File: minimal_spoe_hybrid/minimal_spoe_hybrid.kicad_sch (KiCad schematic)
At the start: 4 parts, among them J1 TBP02R2-381-03BE

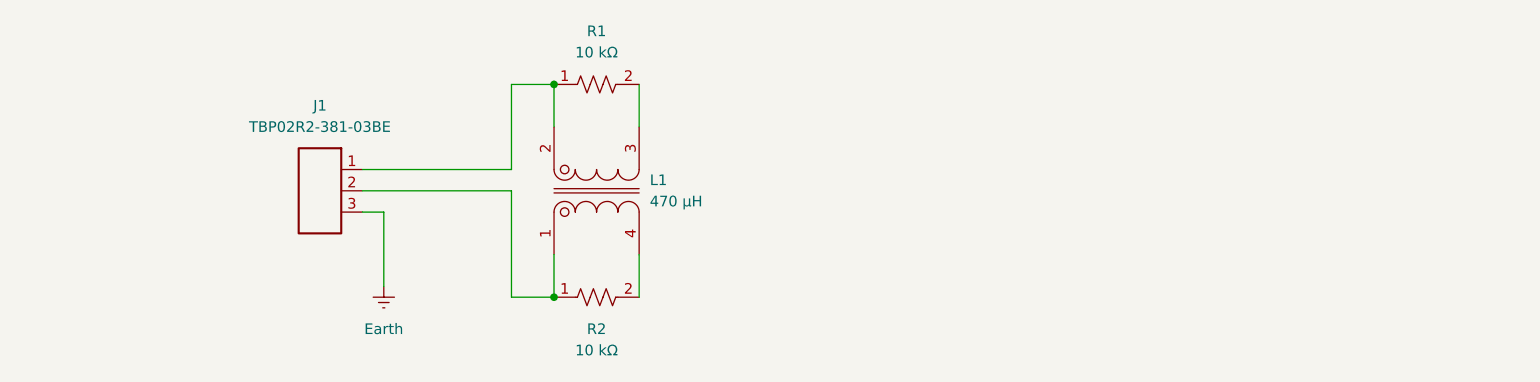
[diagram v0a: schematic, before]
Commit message: Update KiCAD Symbol Generator submodule and modify project settings
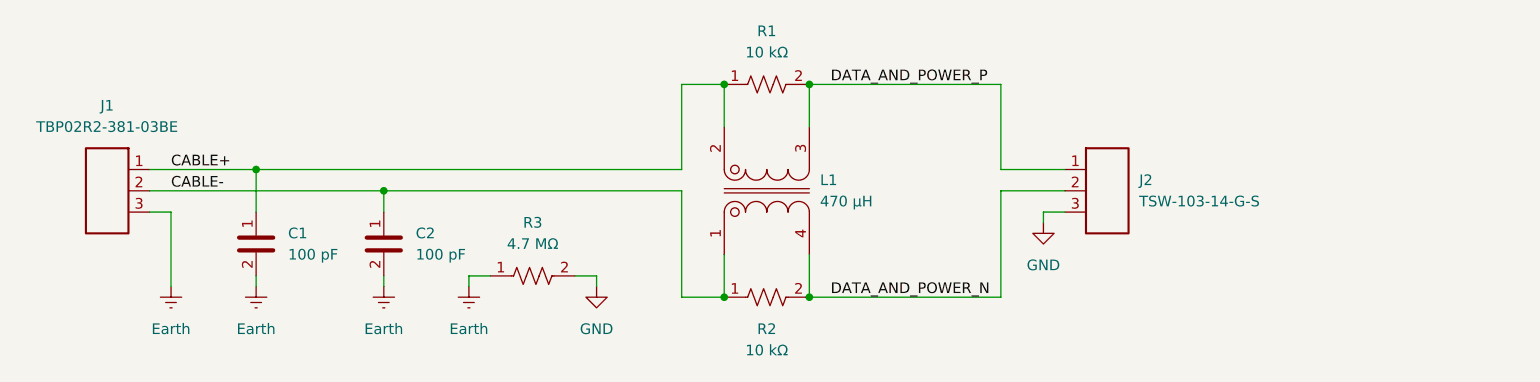
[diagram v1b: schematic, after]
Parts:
- added C1, C2: 100 pF, capacitor_footprints:C_1812_4532Metric, symbol UNITED_CAPACITORS_DATA_BASE:C_C1812C101JHGACTU
- added J2: TSW-103-14-G-S, connector_footprints:TSW-103-14-G-S, symbol UNITED_CONNECTORS_DATA_BASE:J_TSW-103-14-G-S
- added R3: 4.7 MΩ, resistor_footprints:R_2010_5025Metric, symbol UNITED_RESISTORS_DATA_BASE:R_CHV2010-JW-475ELF
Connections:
- net Earth: now also C1.2, C2.2, R3.1
- net CABLE-: now reaches J1.2, L1.1, R2.1
- net CABLE-: now also C2.1
- net DATA_AND_POWER_P: now reaches L1.2, R1.2
- net DATA_AND_POWER_P: now also J2.1
- net CABLE+: now reaches J1.1, L1.3, R1.1
- net CABLE+: now also C1.1
- net DATA_AND_POWER_N: now reaches L1.4, R2.2
- net DATA_AND_POWER_N: now also J2.2
- new net GND: J2.3, R3.2
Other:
- moved on the sheet: J1, L1, R1, R2

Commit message: Update KiCAD Symbol Generator submodule and modify project configuration
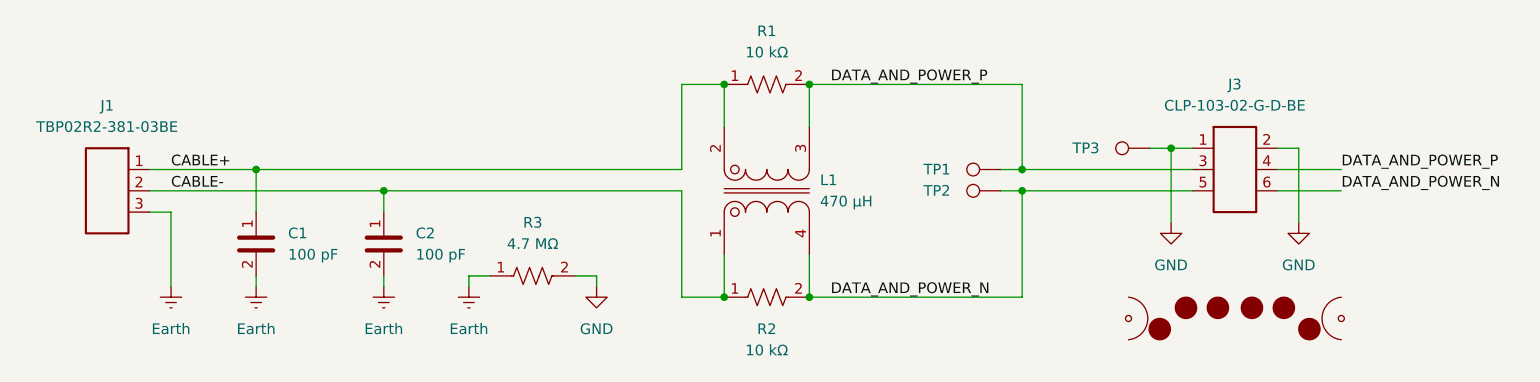
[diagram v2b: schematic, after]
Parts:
- removed J2: TSW-103-14-G-S, connector_footprints:TSW-103-14-G-S, symbol UNITED_CONNECTORS_DATA_BASE:J_TSW-103-14-G-S
- added J3: CLP-103-02-G-D-BE, connector_footprints:CLP-103-02-G-D-BE, symbol UNITED_CONNECTORS_DATA_BASE:J_CLP-103-02-G-D-BE
- added MB1: mouse-bite-midle-50mil-200mil, mouse_bite_footprints:mouse-bite-midle-50mil-250mil, symbol UNITED_MOUSE_BITES_DATA_BASE:mouse-bite-midle-50mil-250mil
- added TP1, TP2, TP3: TestPoint, test_point_footprints:TestPoint_THTPad_Castelated, symbol UNITED_TEST_POINTS:TestPoint_Castelated
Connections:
- net DATA_AND_POWER_N: now also J3.5, J3.6, TP2.1
- net DATA_AND_POWER_P: now also J3.3, J3.4, TP1.1
- net GND: now also J3.1, J3.2, TP3.1

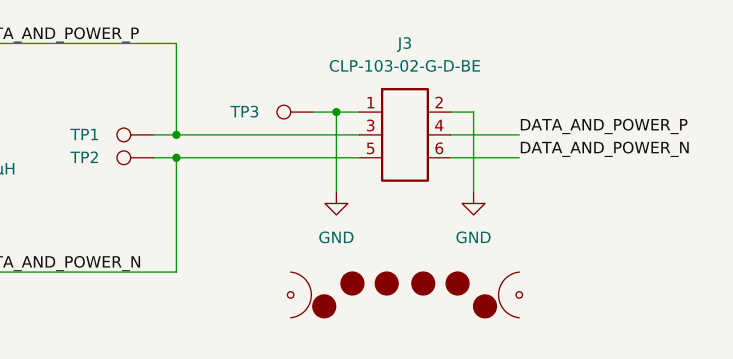
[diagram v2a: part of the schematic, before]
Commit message: Update KiCAD Symbol Generator submodule and remove unused circle elements from schematic
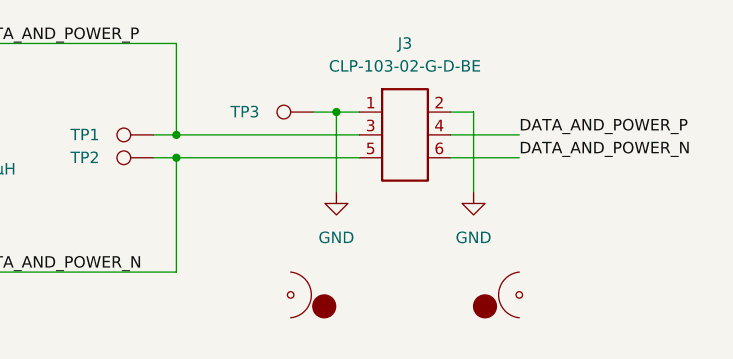
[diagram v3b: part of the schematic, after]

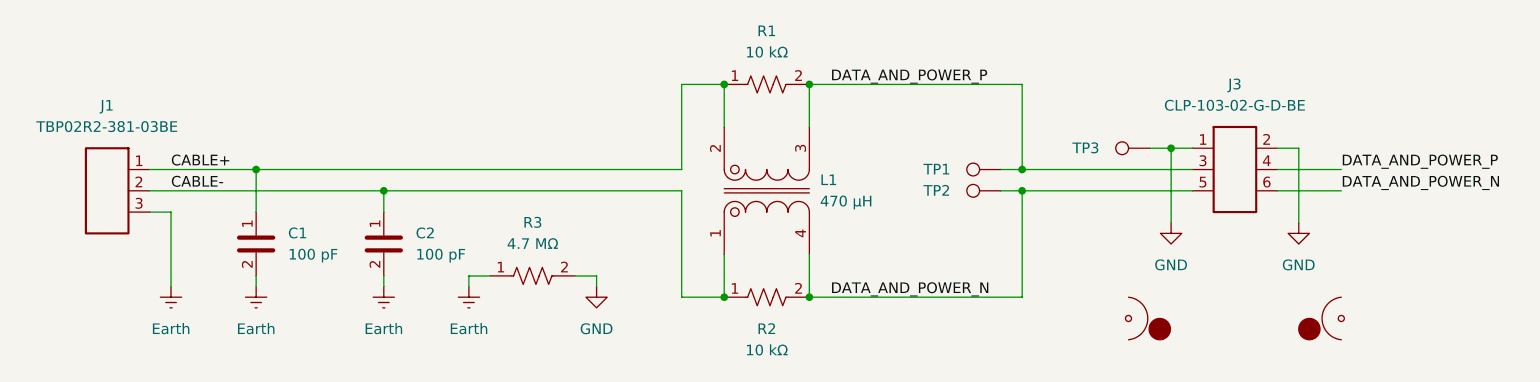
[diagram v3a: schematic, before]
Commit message: Update KiCAD Symbol Generator submodule and regenerate PDF schematic
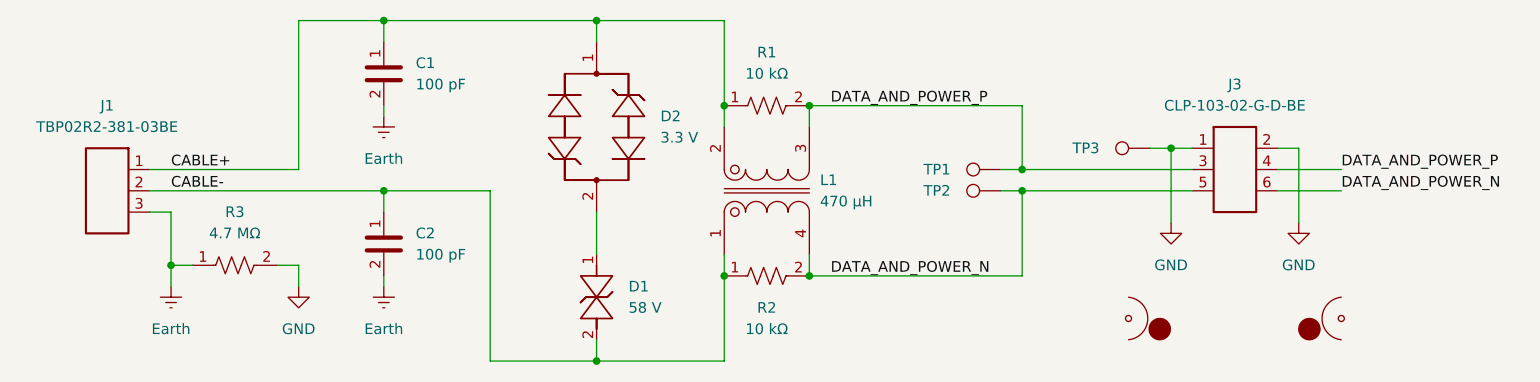
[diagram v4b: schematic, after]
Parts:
- added D1: 58 V, diode_footprints:DO-214AA, symbol UNITED_DIODES_DATA_BASE:D_SMBJ58CA
- added D2: 3.3 V, diode_footprints:SOD323, symbol UNITED_DIODES_DATA_BASE:D_SP4020-01FTG-C
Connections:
- net CABLE+: now also D2.1
- net CABLE-: now also D1.2
- new net: D1.1, D2.2
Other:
- moved on the sheet: C1, R1, R2, R3

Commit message: Add minimal_spoe_hybrid.glb and update KiCAD Symbol Generator submodule
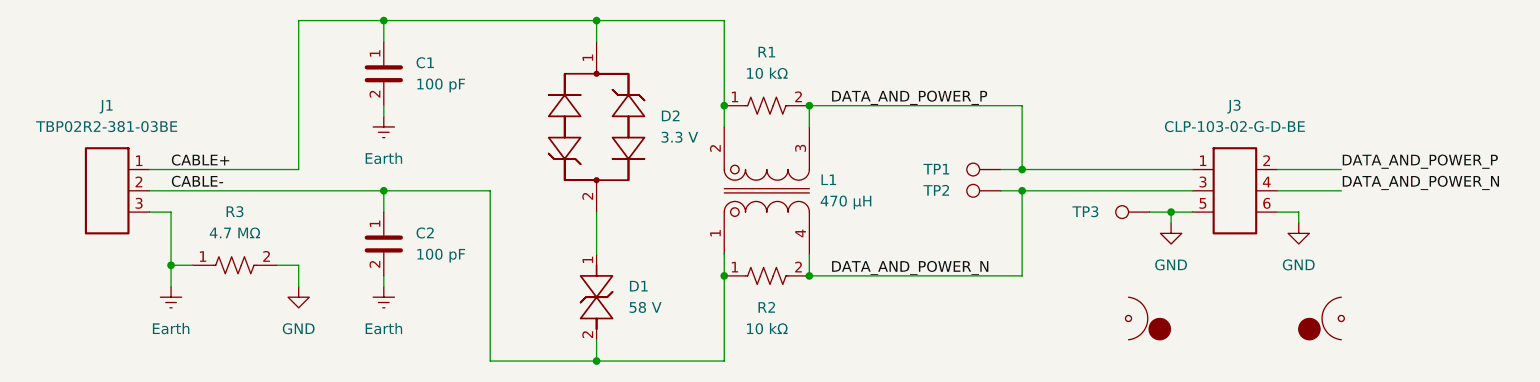
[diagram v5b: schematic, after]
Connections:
- net DATA_AND_POWER_N: now also J3.3, J3.4; no longer J3.5, J3.6
- net DATA_AND_POWER_P: now also J3.1, J3.2; no longer J3.3, J3.4
- net GND: now also J3.5, J3.6; no longer J3.1, J3.2
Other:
- moved on the sheet: J3, TP3
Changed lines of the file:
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@@
-	)
-	(junction
-		(at 195.58 96.52)
-		(diameter 0)
-		(color 0 0 0 0)
 	)
 	(junction
@@
 	)
 	(junction
+		(at 195.58 104.14)
+		(diameter 0)
+		(color 0 0 0 0)
+	)
+	(junction
 		(at 142.24 91.44)
 		(diameter 0)
@@
 	(wire
 		(pts
+			(xy 195.58 104.14) (xy 195.58 105.41)
+		)
+		(stroke
+			(width 0)
+			(type default)
+		)
+	)
+	(wire
+		(pts
 			(xy 101.6 91.44) (xy 101.6 92.71)
 		)
@@
 	(wire
 		(pts
+			(xy 208.28 104.14) (xy 210.82 104.14)
+		)
+		(stroke
+			(width 0)
+			(type default)
+		)
+	)
+	(wire
+		(pts
 			(xy 101.6 104.14) (xy 101.6 101.6)
 		)
@@
 	(wire
 		(pts
-			(xy 193.04 96.52) (xy 195.58 96.52)
-		)
-		(stroke
-			(width 0)
-			(type default)
-		)
-	)
-	(wire
-		(pts
 			(xy 127 121.92) (xy 142.24 121.92)
 		)
@@
 	(wire
 		(pts
+			(xy 195.58 104.14) (xy 198.12 104.14)
+		)
+		(stroke
+			(width 0)
+			(type default)
+		)
+	)
+	(wire
+		(pts
 			(xy 177.8 99.06) (xy 198.12 99.06)
 		)
@@
 	(wire
 		(pts
-			(xy 210.82 96.52) (xy 208.28 96.52)
-		)
-		(stroke
-			(width 0)
-			(type default)
-		)
-	)
-	(wire
-		(pts
-			(xy 195.58 96.52) (xy 195.58 105.41)
-		)
-		(stroke
-			(width 0)
-			(type default)
-		)
-	)
-	(wire
-		(pts
-			(xy 198.12 96.52) (xy 195.58 96.52)
+			(xy 193.04 104.14) (xy 195.58 104.14)
 		)
 		(stroke
@@
 	(wire
 		(pts
-			(xy 210.82 105.41) (xy 210.82 96.52)
+			(xy 210.82 105.41) (xy 210.82 104.14)
 		)
 		(stroke
@@
 	(symbol
 		(lib_id "UNITED_CONNECTORS_DATA_BASE:J_CLP-103-02-G-D-BE")
-		(at 203.2 99.06 0)
+		(at 203.2 101.6 0)
 		(unit 1)
 		(exclude_from_sim no)
@@
 		(fields_autoplaced yes)
 		(property "Reference" "J3"
-			(at 203.2 88.9 0)
+			(at 203.2 91.44 0)
 			(effects
 				(font
@@
 		)
 		(property "Value" "CLP-103-02-G-D-BE"
-			(at 203.2 91.44 0)
+			(at 203.2 93.98 0)
 			(effects
 				(font
@@
 		)
 		(property "Footprint" "connector_footprints:CLP-103-02-G-D-BE"
-			(at 208.28 107.95 0)
+			(at 208.28 110.49 0)
 			(show_name yes)
 			(effects
@@
 		)
 		(property "Datasheet" "https://suddendocs.samtec.com/catalog_english/clp_sm.pdf?_gl=1*1y4jlr9*_gcl_au*MTM0MTYyNTQ5MS4xNzM2MDk5MTUz*_ga*MTYxNDYyMTQ0Mi4xNzM2MDk5MTUz*_ga_3KFNZC07WW*MTczNjY4MDQ4OS4xNS4xLjE3MzY2ODEzNzcuNjAuMC4w"
-			(at 208.28 110.49 0)
+			(at 208.28 113.03 0)
 			(show_name yes)
 			(effects
@@
 		)
 		(property "Description" "Samtec CLP-1xx-02-G-D-BE series,  3 positions connector,  1.27 mm pitch,  Black,  Vertical mounting,  5.2 A,  300 V,  Surface Mount,  Tin plated"
-			(at 208.28 113.03 0)
+			(at 208.28 115.57 0)
 			(show_name yes)
 			(effects
@@
 		)
 		(property "Color" "Black"
-			(at 208.28 115.57 0)
+			(at 208.28 118.11 0)
 			(show_name yes)
 			(effects
@@
 		)
 		(property "Contact Plating" "Tin"
-			(at 208.28 118.11 0)
+			(at 208.28 120.65 0)
 			(show_name yes)
 			(effects
@@
 		)
 		(property "Current Rating (A)" "5.2"
-			(at 208.28 120.65 0)
+			(at 208.28 123.19 0)
 			(show_name yes)
 			(effects
@@
 		)
 		(property "MPN" "CLP-103-02-G-D-BE"
-			(at 208.28 123.19 0)
+			(at 208.28 125.73 0)
 			(show_name yes)
 			(effects
@@
 		)
 		(property "Manufacturer" "Samtec"
-			(at 208.28 125.73 0)
+			(at 208.28 128.27 0)
 			(show_name yes)
 			(effects
@@
 		)
 		(property "Mounting Angle" "Vertical"
-			(at 208.28 128.27 0)
+			(at 208.28 130.81 0)
 			(show_name yes)
 			(effects
@@
 		)
 		(property "Mounting Style" "Surface Mount"
-			(at 208.28 130.81 0)
+			(at 208.28 133.35 0)
 			(show_name yes)
 			(effects
@@
 		)
 		(property "Number of Rows" "2"
-			(at 208.28 133.35 0)
+			(at 208.28 135.89 0)
 			(show_name yes)
 			(effects
@@
 		)
 		(property "Pin Count" "3"
-			(at 208.28 135.89 0)
+			(at 208.28 138.43 0)
 			(show_name yes)
 			(effects
@@
 		)
 		(property "Pitch (mm)" "1.27"
-			(at 208.28 138.43 0)
+			(at 208.28 140.97 0)
 			(show_name yes)
 			(effects
@@
 		)
 		(property "Series" "CLP-1xx-02-G-D-BE"
-			(at 208.28 140.97 0)
+			(at 208.28 143.51 0)
 			(show_name yes)
 			(effects
@@
 		)
 		(property "Symbol Name" "J_CLP-103-02-G-D-BE"
-			(at 208.28 143.51 0)
+			(at 208.28 146.05 0)
 			(show_name yes)
 			(effects
@@
 		)
 		(property "Trustedparts Search" "https://www.trustedparts.com/en/search/CLP-103-02-G-D-BE"
-			(at 208.28 146.05 0)
+			(at 208.28 148.59 0)
 			(show_name yes)
 			(effects
@@
 		)
 		(property "Voltage Rating (V)" "300"
-			(at 208.28 148.59 0)
+			(at 208.28 151.13 0)
 			(show_name yes)
 			(effects
@@
 	(symbol
 		(lib_id "UNITED_TEST_POINTS:TestPoint_Castelated")
-		(at 193.04 96.52 90)
+		(at 193.04 104.14 90)
 		(unit 1)
 		(exclude_from_sim no)
@@
 		(dnp no)
 		(property "Reference" "TP3"
-			(at 185.42 96.52 90)
+			(at 185.42 104.14 90)
 			(effects
 				(font
@@
 		)
 		(property "Value" "TestPoint"
-			(at 190.5 93.98 0)
+			(at 190.5 101.6 0)
 			(effects
 				(font
@@
 		)
 		(property "Footprint" "test_point_footprints:TestPoint_THTPad_Castelated"
-			(at 198.12 93.98 0)
+			(at 198.12 101.6 0)
 			(effects
 				(font
@@
 		)
 		(property "Datasheet" "~"
-			(at 193.04 93.98 0)
+			(at 193.04 101.6 0)
 			(effects
 				(font
@@
 		)
 		(property "Description" "test point"
-			(at 195.58 93.98 0)
-			(effects
-				(font
+			(at 195.58 101.6 0)
+			(effects
+				(font

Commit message: Switch to KiCad 9
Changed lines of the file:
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@@
 (kicad_sch
-	(version 20231120)
+	(version 20250114)
 	(generator "eeschema")
-	(generator_version "8.0")
+	(generator_version "9.0")
 	(paper "A4")
 	(junction
@@
 		)
 	)
+	(embedded_fonts no)
 )
